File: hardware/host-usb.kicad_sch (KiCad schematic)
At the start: 24 parts, among them IC10 DSC6101CI2A-024.0000, IC8 24LC128, IC9 CY7C68013A-56PVXC

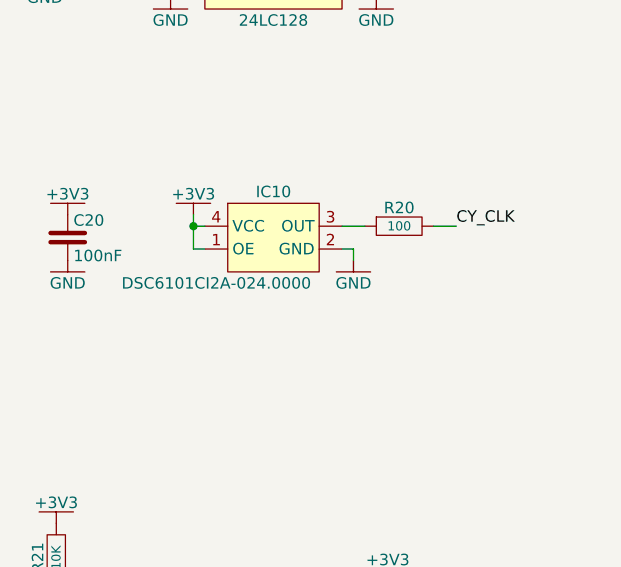
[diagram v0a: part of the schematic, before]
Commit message: replace obsolete components, updated PCB, schematics and production files
Signed-off-by: Jakub Sobota <jakub.sobota@3mdeb.com>
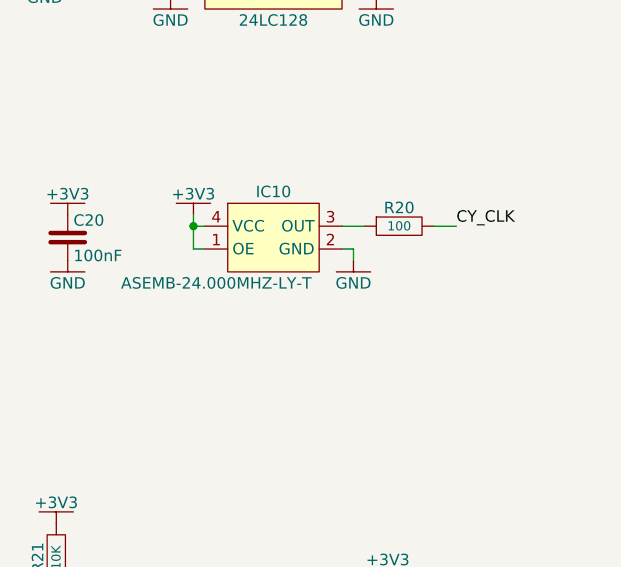
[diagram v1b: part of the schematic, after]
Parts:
- IC10: value DSC6101CI2A-024.0000 -> ASEMB-24.000MHZ-LY-T
